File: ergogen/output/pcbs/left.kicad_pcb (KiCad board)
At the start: 2 copper layers, 130 x 99.4 mm, 28 parts

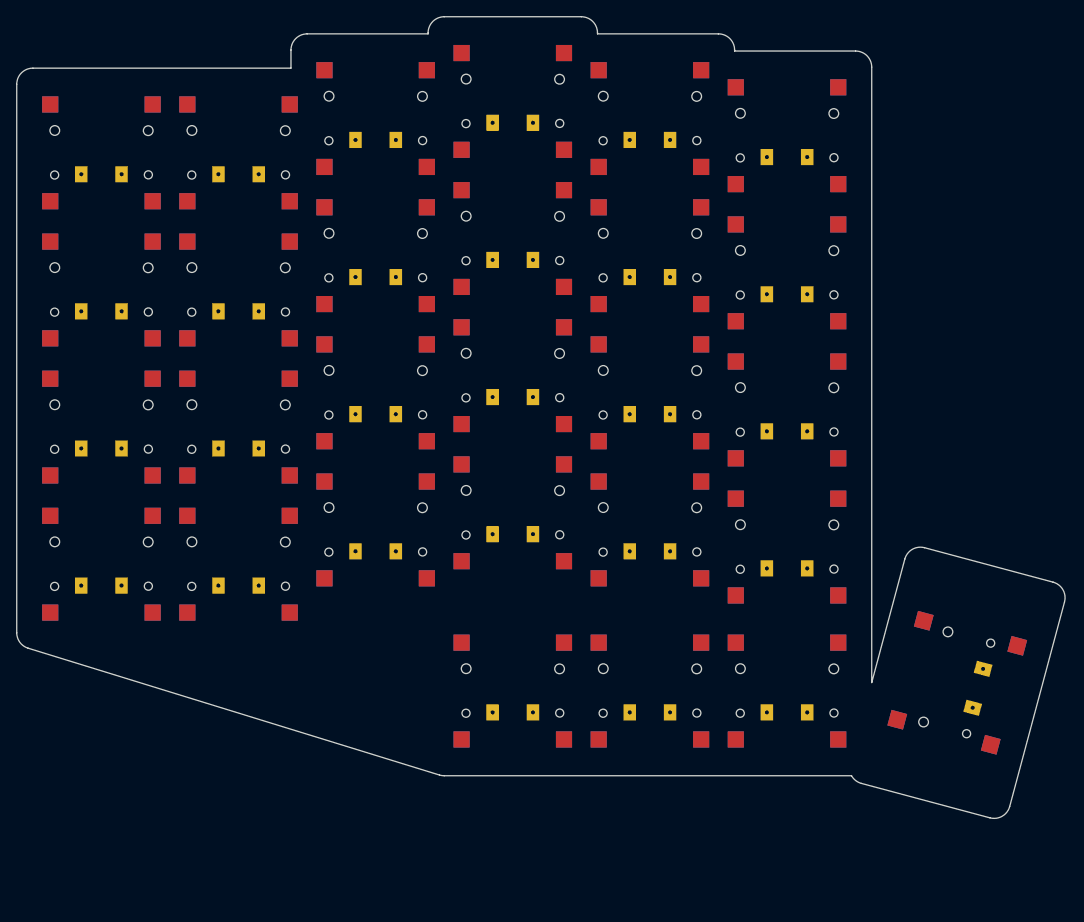
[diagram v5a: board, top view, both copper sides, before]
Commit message: feat: diodes and mcu cover
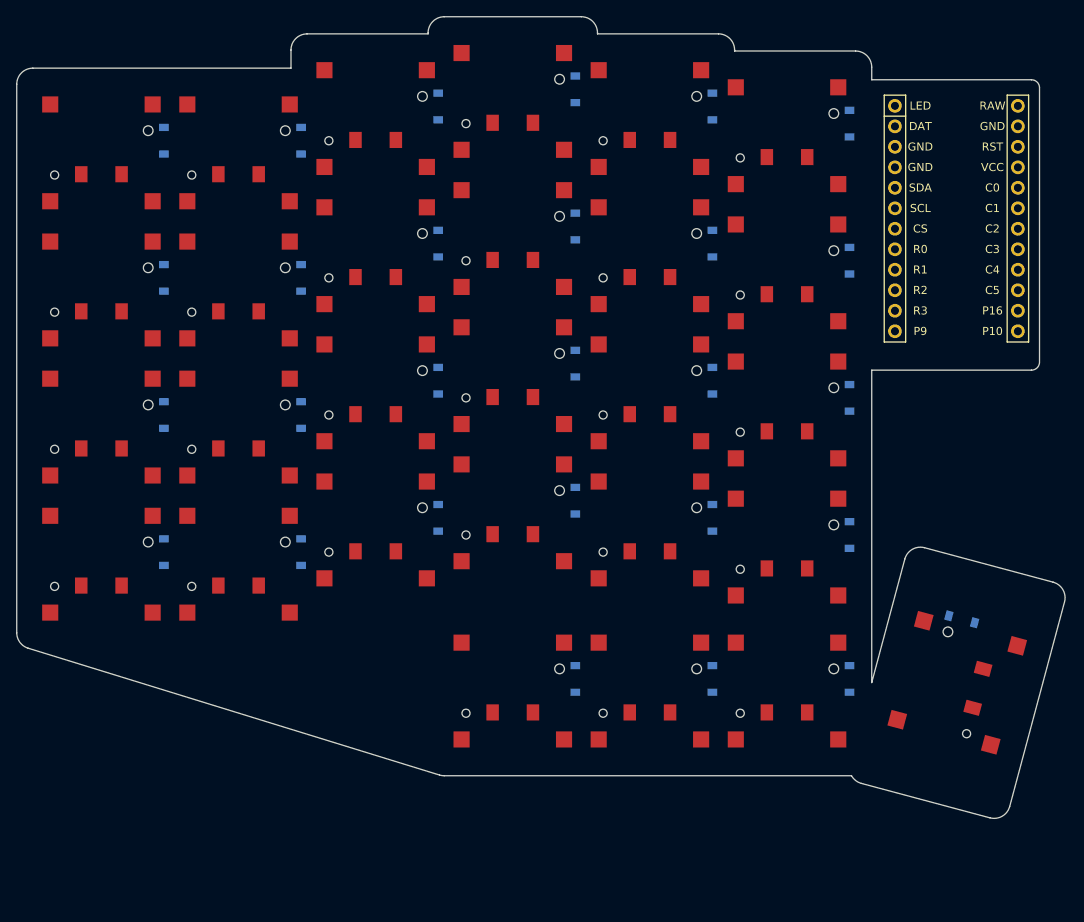
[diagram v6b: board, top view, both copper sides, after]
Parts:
- added D1: , ceoloide:diode_tht_sod123, B.Cu at (107.8, 98.5)
- added D10: , ceoloide:diode_tht_sod123, B.Cu at (141.8, 77.2)
- added D11: , ceoloide:diode_tht_sod123, B.Cu at (141.8, 60.2)
- added D12: , ceoloide:diode_tht_sod123, B.Cu at (141.8, 43.2)
- added D13: , ceoloide:diode_tht_sod123, B.Cu at (158.8, 92.1)
- added D14: , ceoloide:diode_tht_sod123, B.Cu at (158.8, 75.1)
- added D15: , ceoloide:diode_tht_sod123, B.Cu at (158.8, 58.1)
- added D16: , ceoloide:diode_tht_sod123, B.Cu at (158.8, 41.1)
- added D17: , ceoloide:diode_tht_sod123, B.Cu at (175.8, 94.2)
- added D18: , ceoloide:diode_tht_sod123, B.Cu at (175.8, 77.2)
- added D19: , ceoloide:diode_tht_sod123, B.Cu at (175.8, 60.2)
- added D2: , ceoloide:diode_tht_sod123, B.Cu at (107.8, 81.5)
- added D20: , ceoloide:diode_tht_sod123, B.Cu at (175.8, 43.2)
- added D21: , ceoloide:diode_tht_sod123, B.Cu at (192.8, 96.4)
- added D22: , ceoloide:diode_tht_sod123, B.Cu at (192.8, 79.4)
- added D23: , ceoloide:diode_tht_sod123, B.Cu at (192.8, 62.4)
- added D24: , ceoloide:diode_tht_sod123, B.Cu at (192.8, 45.4)
- added D25: , ceoloide:diode_tht_sod123, B.Cu at (158.8, 114.2)
- added D26: , ceoloide:diode_tht_sod123, B.Cu at (175.8, 114.2)
- added D27: , ceoloide:diode_tht_sod123, B.Cu at (192.8, 114.2)
- added D28: , ceoloide:diode_tht_sod123, B.Cu at (206.7, 106.8)
- added D3: , ceoloide:diode_tht_sod123, B.Cu at (107.8, 64.5)
- added D4: , ceoloide:diode_tht_sod123, B.Cu at (107.8, 47.5)
- added D5: , ceoloide:diode_tht_sod123, B.Cu at (124.8, 98.5)
- added D6: , ceoloide:diode_tht_sod123, B.Cu at (124.8, 81.5)
- added D7: , ceoloide:diode_tht_sod123, B.Cu at (124.8, 64.5)
- added D8: , ceoloide:diode_tht_sod123, B.Cu at (124.8, 47.5)
- added D9: , ceoloide:diode_tht_sod123, B.Cu at (141.8, 94.2)
- added MCU1: , ceoloide:mcu_nice_nano, F.Cu at (206.0, 55.9)
- S1, S10, S11, S12, S13, S14, S15, S16, S17, S18, S19, S2, S20, S21, S22, S23, S24, S25, S26, S27, S28, S3, S4, S5, S6, S7, S8, S9: footprint CPG1316S01D02_reversible -> CPG1316S01D02_mikeholscher
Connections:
- S1 pad 1: C0 -> outer_bottom
- S1 pad 2: outer_bottom -> C0
- S10 pad 1: C2 -> ring_home
- S10 pad 2: ring_home -> C2
- S11 pad 1: C2 -> ring_top
- S11 pad 2: ring_top -> C2
- S12 pad 1: C2 -> ring_number
- S12 pad 2: ring_number -> C2
- S13 pad 1: C3 -> middle_bottom
- S13 pad 2: middle_bottom -> C3
- S14 pad 1: C3 -> middle_home
- S14 pad 2: middle_home -> C3
- S15 pad 1: C3 -> middle_top
- S15 pad 2: middle_top -> C3
- S16 pad 1: C3 -> middle_number
- S16 pad 2: middle_number -> C3
- S17 pad 1: C4 -> index_bottom
- S17 pad 2: index_bottom -> C4
- S18 pad 1: C4 -> index_home
- S18 pad 2: index_home -> C4
- S19 pad 1: C4 -> index_top
- S19 pad 2: index_top -> C4
- S2 pad 1: C0 -> outer_home
- S2 pad 2: outer_home -> C0
- S20 pad 1: C4 -> index_number
- S20 pad 2: index_number -> C4
- S21 pad 1: C5 -> inner_bottom
- S21 pad 2: inner_bottom -> C5
- S22 pad 1: C5 -> inner_home
- S22 pad 2: inner_home -> C5
- S23 pad 1: C5 -> inner_top
- S23 pad 2: inner_top -> C5
- S24 pad 1: C5 -> inner_number
- S24 pad 2: inner_number -> C5
- S25 pad 1: C2 -> inward_home
- S25 pad 2: inward_home -> C2
- S26 pad 1: C3 -> outward_home
- S26 pad 2: outward_home -> C3
- S27 pad 1: C4 -> small_thumbkey_home
- S27 pad 2: small_thumbkey_home -> C4
- S28 pad 1: C5 -> thumbkey_home
- S28 pad 2: thumbkey_home -> C5
- S3 pad 1: C0 -> outer_top
- S3 pad 2: outer_top -> C0
- S4 pad 1: C0 -> outer_number
- S4 pad 2: outer_number -> C0
- S5 pad 1: C1 -> pinky_bottom
- S5 pad 2: pinky_bottom -> C1
- S6 pad 1: C1 -> pinky_home
- S6 pad 2: pinky_home -> C1
- S7 pad 1: C1 -> pinky_top
- S7 pad 2: pinky_top -> C1
- S8 pad 1: C1 -> pinky_number
- S8 pad 2: pinky_number -> C1
- S9 pad 1: C2 -> ring_bottom
- S9 pad 2: ring_bottom -> C2
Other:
- outline, holes or cut-outs redrawn

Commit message: feat: reset and battery footprints
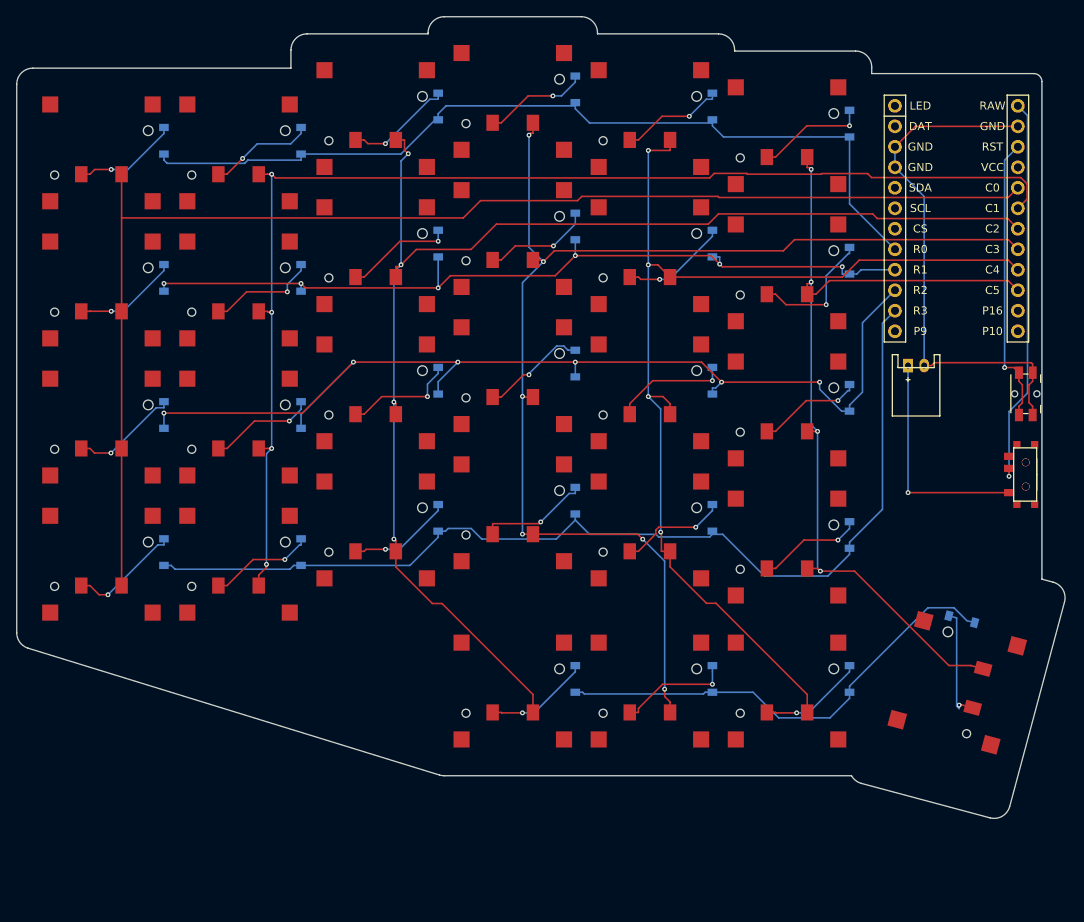
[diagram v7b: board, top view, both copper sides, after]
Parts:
- added B1: Panasonic_EVQPUL_EVQPUC, Panasonic_EVQPUL_EVQPUC, F.Cu at (214.6, 78.9)
- added JST1: , JST_PH_S2B-PH-K_02x2.00mm_Angled, F.Cu at (201.0, 75.4)
- added T1: , E73:SPDT_C128955, F.Cu at (214.6, 88.9)
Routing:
- net C2: track 0.00 -> 164.4 mm, vias 0 -> 4
- net C0: track 0.00 -> 163.8 mm
- net C1: track 0.00 -> 154.7 mm, vias 0 -> 4
- net C3: track 0.00 -> 154.4 mm, vias 0 -> 6
- net C4: track 0.00 -> 135.3 mm, vias 0 -> 4
- net R2: track 0.00 -> 129.7 mm, vias 0 -> 6
- net R3: track 0.00 -> 127.2 mm
- net C5: track 0.00 -> 109.5 mm, vias 0 -> 4
- net R0: track 0.00 -> 109.0 mm
- net R1: track 0.00 -> 103.7 mm, vias 0 -> 6
- net GND: track 0.00 -> 65.3 mm
- net R4: track 0.00 -> 58.2 mm
- net RAW: track 0.00 -> 48.3 mm, vias 0 -> 1
- net RST: track 0.00 -> 35.7 mm, vias 0 -> 1
- net pos: track 0.00 -> 28.3 mm, vias 0 -> 1
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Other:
- outline, holes or cut-outs redrawn
